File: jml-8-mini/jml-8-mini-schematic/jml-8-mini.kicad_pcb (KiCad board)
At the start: 2 copper layers, 133.1 x 80.5 mm, 47 parts, among them J1 BarrelJack, J2 SIO CHB, J3 UART, J4 CTC Extra Lines, J5 Address Decoding, J6 Z80 Lines, SW1 Reset, SW2 Power, U1 Z80CPU, U10 74LS74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

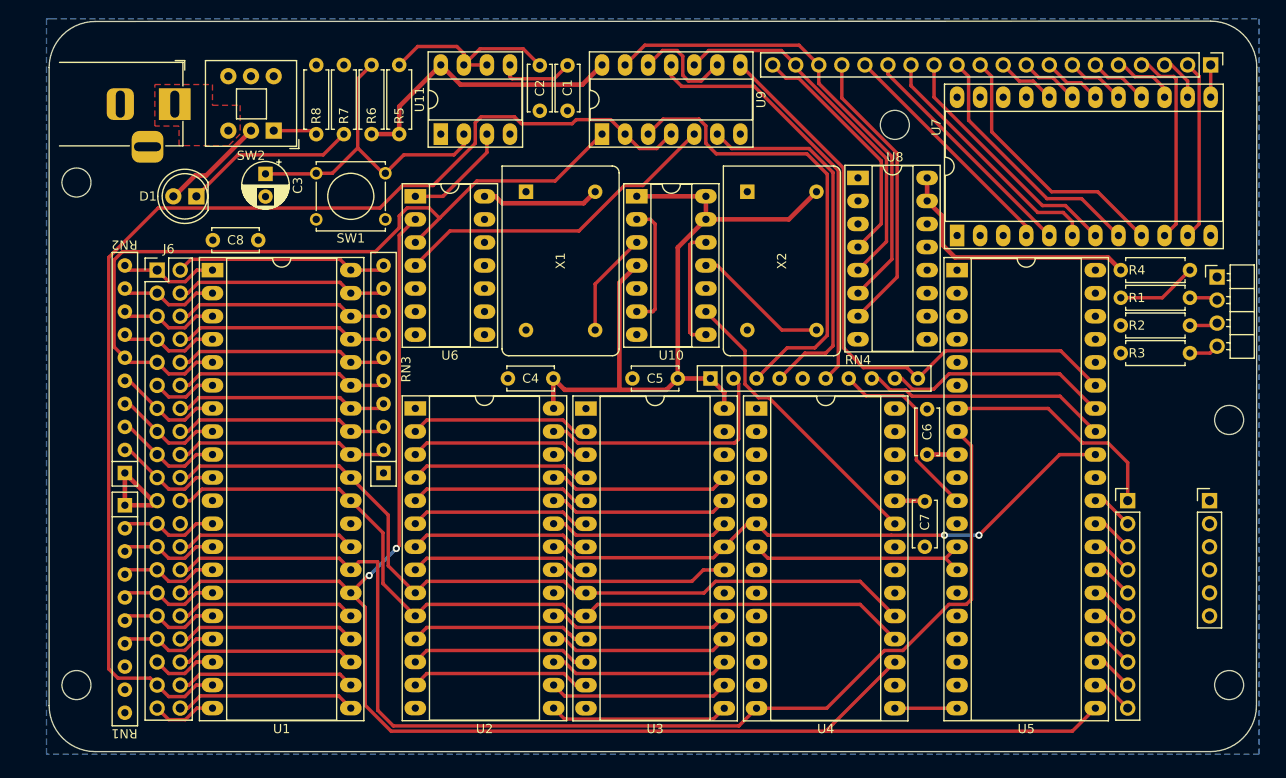
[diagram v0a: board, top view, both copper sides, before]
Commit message: making pcb 4 layers instead of 2, restarting routing, more exact outline dimensions
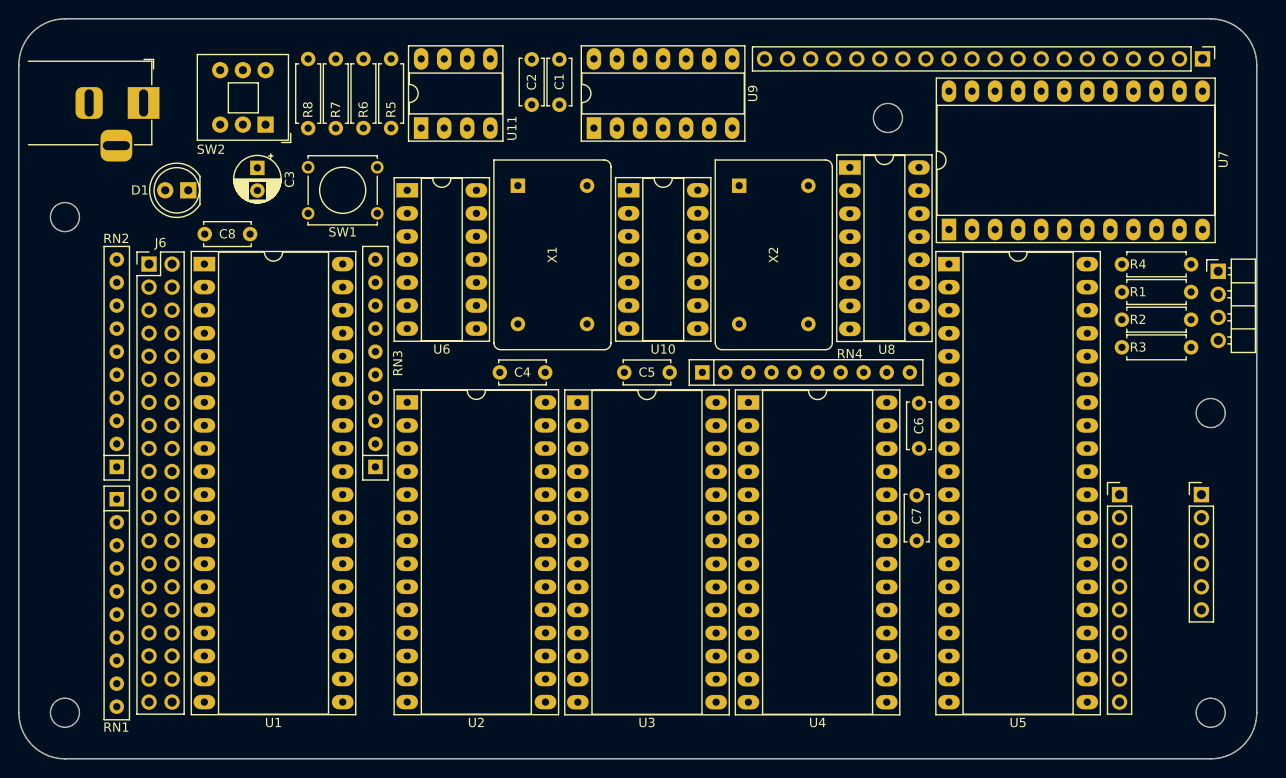
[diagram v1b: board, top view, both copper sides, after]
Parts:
- moved H3 4.02 mm to (88.9, 71.9)
- moved H5 3.66 mm to (215.1, 126.5)
- moved J1 3.44 mm to (97.6, 59.3)
- moved H4 3.30 mm to (88.9, 126.5)
- moved U11 2.26 mm to (128.1, 62.1)
- moved H1 2.17 mm to (215.1, 93.5)
- moved U8 1.45 mm to (175.4, 66.4)
- moved C4 1.11 mm to (141.8, 89.0)
- moved C5 1.11 mm to (155.5, 89.0)
- moved J6 1.11 mm to (98.2, 77.1)
- moved RN1 1.11 mm to (94.6, 103.0)
- moved RN4 1.11 mm to (159.1, 89.0)
- moved U1 1.11 mm to (104.3, 77.1)
- moved U3 1.11 mm to (145.4, 92.3)
- moved U4 1.11 mm to (164.2, 92.3)
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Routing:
- net +5V: track 186.9 -> 0.00 mm
- net /~{RESET}: track 170.5 -> 0.00 mm, vias 2 -> 0
- net /~{MREQ}: track 130.8 -> 0.00 mm
- net /~{M1}: track 130.6 -> 0.00 mm
- net /A0: track 118.6 -> 0.00 mm
- net /A1: track 116.4 -> 0.00 mm
- net /A15: track 87.2 -> 0.00 mm
- net /~{RD}: track 85.8 -> 0.00 mm, vias 2 -> 0
- net /~{SIO}: track 67.9 -> 0.00 mm
- net /Address Decoding/Q2: track 53.2 -> 0.00 mm
- net /~{ROM}: track 51.6 -> 0.00 mm
- net /~{CTC}: track 47.4 -> 0.00 mm
- net /A5: track 43.5 -> 0.00 mm
- net /A3: track 43.5 -> 0.00 mm
- net /A7: track 43.5 -> 0.00 mm
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- added copper zone on In2.Cu, net +5V
- added copper zone on In2.Cu, net /Power, Clock and Reset/PWR_IN
- added copper zone on In1.Cu, net GND
- removed copper zone on F.Cu, net /Power, Clock and Reset/PWR_IN
- removed copper zone on B.Cu, net GND
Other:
- board size 133.1 x 80.5 mm -> 136.4 x 81.5 mm
- copper layers 2 -> 4

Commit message: complete PCB routing
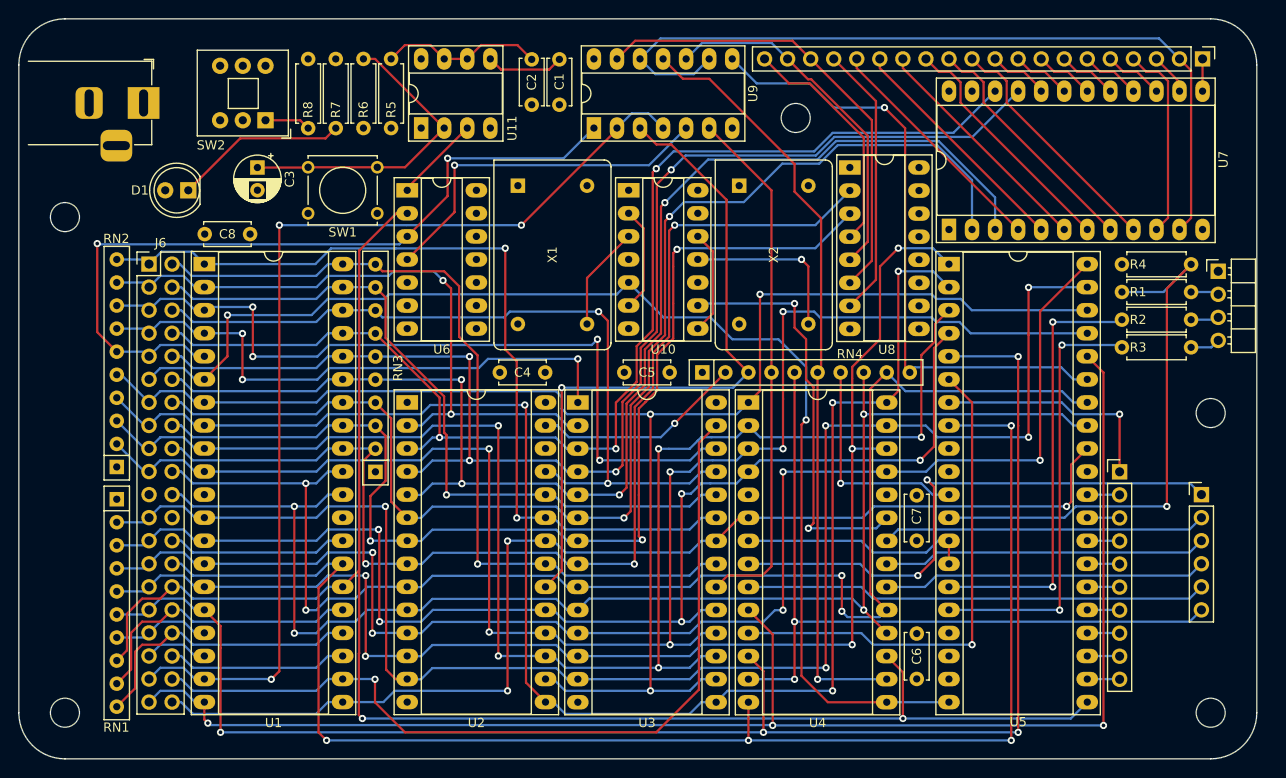
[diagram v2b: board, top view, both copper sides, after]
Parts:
- U4: value Z80 CTC -> Z80CTC
- U5: value Z80 SIO -> Z80SIO
- moved C6 25.4 mm to (182.8, 122.8)
- moved H2 10.2 mm to (169.4, 61.0)
- moved J2 2.51 mm to (205.1, 99.9)
- moved RN3 0.54 mm to (123.1, 99.9)
- moved SW2 0.48 mm to (111.0, 61.2)
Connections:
- J4 pad 1: /Peripherals/CLK/TRG1 -> /Peripherals/ZC/TO1
- J4 pad 2: /Peripherals/ZC/TO1 -> /Peripherals/CLK/TRG1
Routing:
- net /~{RESET}: track 0.00 -> 181.1 mm, vias 0 -> 2
- net /D4: track 0.00 -> 174.3 mm, vias 0 -> 3
- net /D3: track 0.00 -> 174.1 mm, vias 0 -> 4
- net /D6: track 0.00 -> 172.9 mm, vias 0 -> 6
- net /D2: track 0.00 -> 172.4 mm, vias 0 -> 5
- net /~{INT}: track 0.00 -> 171.1 mm, vias 0 -> 4
- net /D5: track 0.00 -> 165.7 mm, vias 0 -> 5
- net /~{IORQ}: track 0.00 -> 163.6 mm, vias 0 -> 3
- net /~{M1}: track 0.00 -> 162.0 mm, vias 0 -> 4
- net /A1: track 0.00 -> 156.1 mm, vias 0 -> 4
- net /A0: track 0.00 -> 154.6 mm, vias 0 -> 4
- net /D0: track 0.00 -> 154.1 mm, vias 0 -> 5
- net /D1: track 0.00 -> 149.2 mm, vias 0 -> 5
- net /A5: track 0.00 -> 148.6 mm, vias 0 -> 4
- net /A6: track 0.00 -> 147.2 mm, vias 0 -> 4
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
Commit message: fix wrong label, add labels and figures to pcb
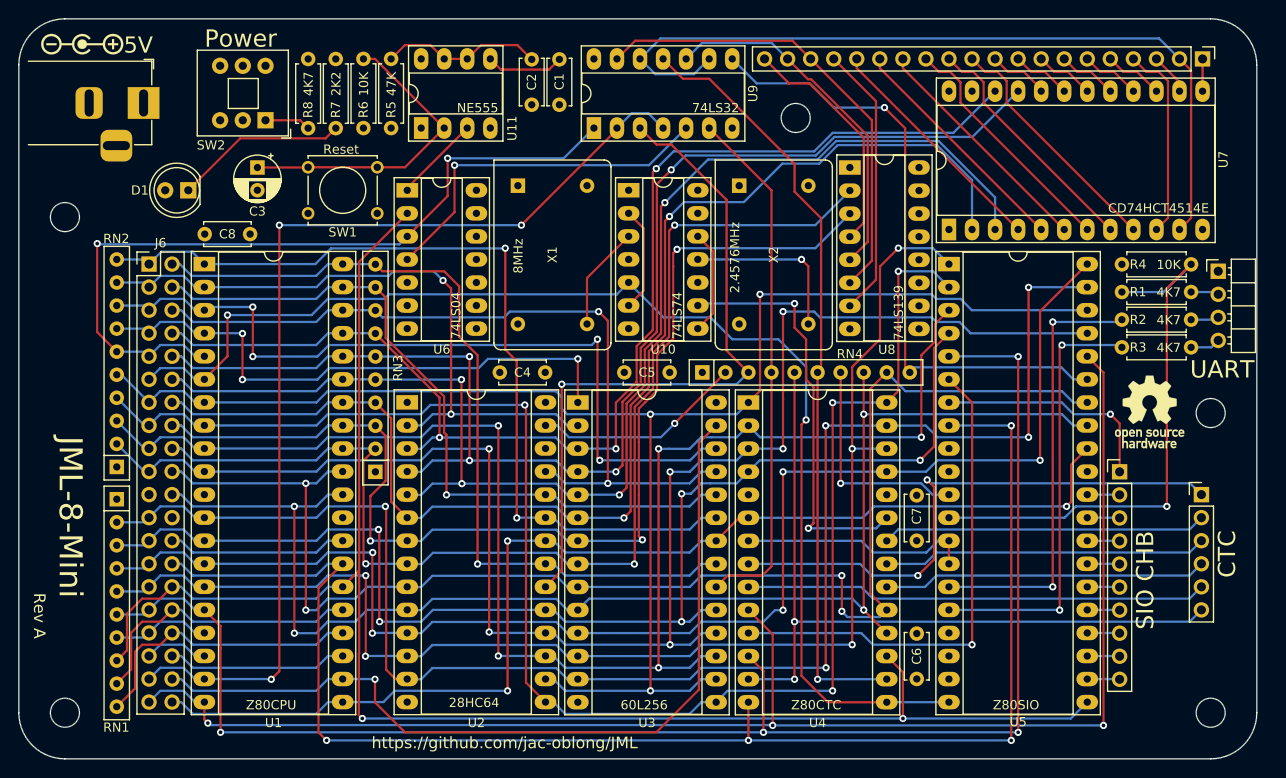
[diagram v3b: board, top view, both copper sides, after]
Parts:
- added REF**: OSHW-Logo_7.5x8mm_SilkScreen, Symbol:OSHW-Logo_7.5x8mm_SilkScreen, F.Cu at (208.4, 93.3)
- added REF**: Polarity_Center_Positive_6mm_SilkScreen, Symbol:Polarity_Center_Positive_6mm_SilkScreen, F.Cu at (90.8, 52.8)
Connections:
- net /Peripherals/CTC_IEO renamed /Peripherals/SIO_IEO
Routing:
- net /~{RESET}: track 181.1 -> 180.4 mm
- net /Peripherals/SIO_IEO: track 25.7 -> 25.1 mm
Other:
- board text added: "1"
- board text added: "10"
- board text added: "10K"
- board text added: "18"
- board text added: "2.4576MHz"
- board text added: "21"
- board text added: "28HC64"
- board text added: "2K2"
- board text added: "30"
- board text added: "47K"
- board text added: "4K7"
- board text added: "5V"
- board text added: "6"
- board text added: "60L256"
- board text added: "7"
- board text added: "74LS04"
- board text added: "74LS139"
- board text added: "74LS32"
- board text added: "74LS74"
- board text added: "8MHz"
- board text added: "CD74HCT4514E"
- board text added: "CTC"
- board text added: "JML-8-Mini"
- board text added: "NE555"
- board text added: "Power"
- board text added: "Reset"
- board text added: "Rev A"
- board text added: "SIO CHB"
- board text added: "UART"
- board text added: "Z80CPU"
- board text added: "Z80CTC"
- board text added: "Z80SIO"
- board text added: "https://github.com/jac-oblong/JML"

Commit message: add JML logo to pcb
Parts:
- added G***: LOGO, LOGO, F.Cu at (88.5, 85.9)
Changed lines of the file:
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@@
     )
+  )
+  (footprint "LOGO" (layer "F.Cu")
+    (at 88.519 85.852 -90)
+    (attr board_only exclude_from_pos_files exclude_from_bom)
+    (fp_text reference "G***" (at 0 0 90) (layer "F.SilkS") hide
+        (effects (font (size 1.5 1.5) (thickness 0.3)))
+    )
+    (fp_text value "LOGO" (at 0.75 0 90) (layer "F.SilkS") hide
+        (effects (font (size 1.5 1.5) (thickness 0.3)))
+    )
+    (fp_poly
+      (pts
+        (xy -4.2 -3.337713)
+        (xy -4.198687 -3.055886)
+        (xy -4.194822 -2.828806)
+        (xy -4.188519 -2.659327)
+        (xy -4.179893 -2.550301)
+        (xy -4.169057 -2.504581)
+        (xy -4.166667 -2.503285)
+        (xy -4.155409 -2.53617)
+        (xy -4.146338 -2.632925)
+        (xy -4.139567 -2.790696)
+        (xy -4.135212 -3.006631)
+        (xy -4.133386 -3.277876)
+        (xy -4.133334 -3.337713)
+        (xy -4.133334 -4.172141)
+        (xy -2.916667 -4.172141)
+        (xy -1.7 -4.172141)
+        (xy -1.7 -3.504599)
+        (xy -1.7 -2.837056)
+        (xy -1.5 -2.837056)
+        (xy -1.3 -2.837056)
+        (xy -1.3 -2.252956)
+        (xy -1.3 -1.668856)
+        (xy -1.066667 -1.668856)
+        (xy -0.833334 -1.668856)
+        (xy -0.833334 -1.084756)
+        (xy -0.833334 -0.500657)
+        (xy -0.6 -0.500657)
+        (xy -0.366667 -0.500657)
+        (xy -0.366667 0.083443)
+        (xy -0.366667 0.667543)
+        (xy -0.016667 0.667543)
+        (xy 0.333333 0.667543)
+        (xy 0.333333 0.083443)
+        (xy 0.333333 -0.500657)
+        (xy 0.566666 -0.500657)
+        (xy 0.8 -0.500657)
+        (xy 0.8 -1.084756)
+        (xy 0.8 -1.668856)
+        (xy 1.033333 -1.668856)
+        (xy 1.266666 -1.668856)
+        (xy 1.266666 -2.252956)
+        (xy 1.266666 -2.837056)
+        (xy 1.45 -2.837056)
+        (xy 1.633333 -2.837056)
+        (xy 1.633333 -3.504599)
+        (xy 1.633333 -4.172141)
+        (xy 2.883333 -4.172141)
+        (xy 4.133333 -4.172141)
+        (xy 4.133333 -3.337713)
+        (xy 4.134647 -3.055886)
+        (xy 4.138512 -2.828806)
+        (xy 4.144814 -2.659327)
+        (xy 4.15344 -2.550301)
+        (xy 4.164276 -2.504581)
+        (xy 4.166666 -2.503285)
+        (xy 4.177924 -2.53617)
+        (xy 4.186996 -2.632925)
+        (xy 4.193766 -2.790696)
+        (xy 4.198121 -3.006631)
+        (xy 4.199948 -3.277876)
+        (xy 4.2 -3.337713)
+        (xy 4.2 -4.172141)
+        (xy 4.766666 -4.172141)
+        (xy 5.333333 -4.172141)
+        (xy 5.333333 -0.834428)
+        (xy 5.333333 2.503286)
+        (xy 7.25 2.503286)
+        (xy 9.166666 2.503286)
+        (xy 9.166666 3.337714)
+        (xy 9.166666 4.172142)
+        (xy 6.683333 4.172142)
+        (xy 4.2 4.172142)
+        (xy 4.2 3.754928)
+        (xy 4.197432 3.574189)
+        (xy 4.190116 3.439781)
+        (xy 4.17863 3.358946)
+        (xy 4.166666 3.337714)
+        (xy 4.152226 3.369847)
+        (xy 4.141487 3.46142)
+        (xy 4.135029 3.605189)
+        (xy 4.133333 3.754928)
+        (xy 4.133333 4.172142)
+        (xy 3.55 4.172142)
+        (xy 2.966666 4.172142)
+        (xy 2.966666 1.251643)
+        (xy 2.966666 -1.668856)
+        (xy 2.7 -1.668856)
+        (xy 2.433333 -1.668856)
+        (xy 2.433333 -1.084756)
+        (xy 2.433333 -0.500657)
+        (xy 2.2 -0.500657)
+        (xy 1.966666 -0.500657)
+        (xy 1.966666 0.083443)
+        (xy 1.966666 0.667543)
+        (xy 1.733333 0.667543)
+        (xy 1.5 0.667543)
+        (xy 1.5 1.251643)
+        (xy 1.5 1.835743)
+        (xy 1.266666 1.835743)
+        (xy 1.033333 1.835743)
+        (xy 1.033333 2.419843)
+        (xy 1.033333 3.003943)
+        (xy 0.8 3.003943)
+        (xy 0.566666 3.003943)
+        (xy 0.566666 3.588042)
+        (xy 0.566666 4.172142)
+        (xy -0.016667 4.172142)
+        (xy -0.6 4.172142)
+        (xy -0.6 3.588042)
+        (xy -0.6 3.003943)
+        (xy -0.833334 3.003943)
+        (xy -1.066667 3.003943)
+        (xy -1.066667 2.419843)
+        (xy -1.066667 1.835743)
+        (xy -1.3 1.835743)
+        (xy -1.533334 1.835743)
+        (xy -1.533334 1.251643)
+        (xy -1.533334 0.667543)
+        (xy -1.766667 0.667543)
+        (xy -2 0.667543)
+        (xy -2 0.083443)
+        (xy -2 -0.500657)
+        (xy -2.233334 -0.500657)
+        (xy -2.466667 -0.500657)
+        (xy -2.466667 -1.084756)
+        (xy -2.466667 -1.668856)
+        (xy -2.733334 -1.668856)
+        (xy -3 -1.668856)
+        (xy -3 1.251643)
+        (xy -3 4.172142)
+        (xy -3.566667 4.172142)
+        (xy -4.133334 4.172142)
+        (xy -4.133334 3.754928)
+        (xy -4.135901 3.574189)
+        (xy -4.143217 3.439781)
+        (xy -4.154704 3.358946)
+        (xy -4.166667 3.337714)
+        (xy -4.181107 3.369847)
+        (xy -4.191846 3.46142)
+        (xy -4.198304 3.605189)
+        (xy -4.2 3.754928)
+        (xy -4.2 4.172142)
+        (xy -6.683334 4.172142)
+        (xy -9.166667 4.172142)
+        (xy -9.166667 3.337714)
+        (xy -9.166667 2.503286)
+        (xy -7.25 2.503286)
+        (xy -5.333334 2.503286)
+        (xy -5.333334 -0.834428)
+        (xy -5.333334 -4.172141)
+        (xy -4.766667 -4.172141)
+        (xy -4.2 -4.172141)
+      )
+      (stroke (width 0) (type solid)) (fill solid) (layer "F.SilkS"))
   )
   (footprint "Resistor_THT:R_Axial_DIN0207_L6.3mm_D2.5mm_P7.62mm_Horizontal" (layer "F.Cu")

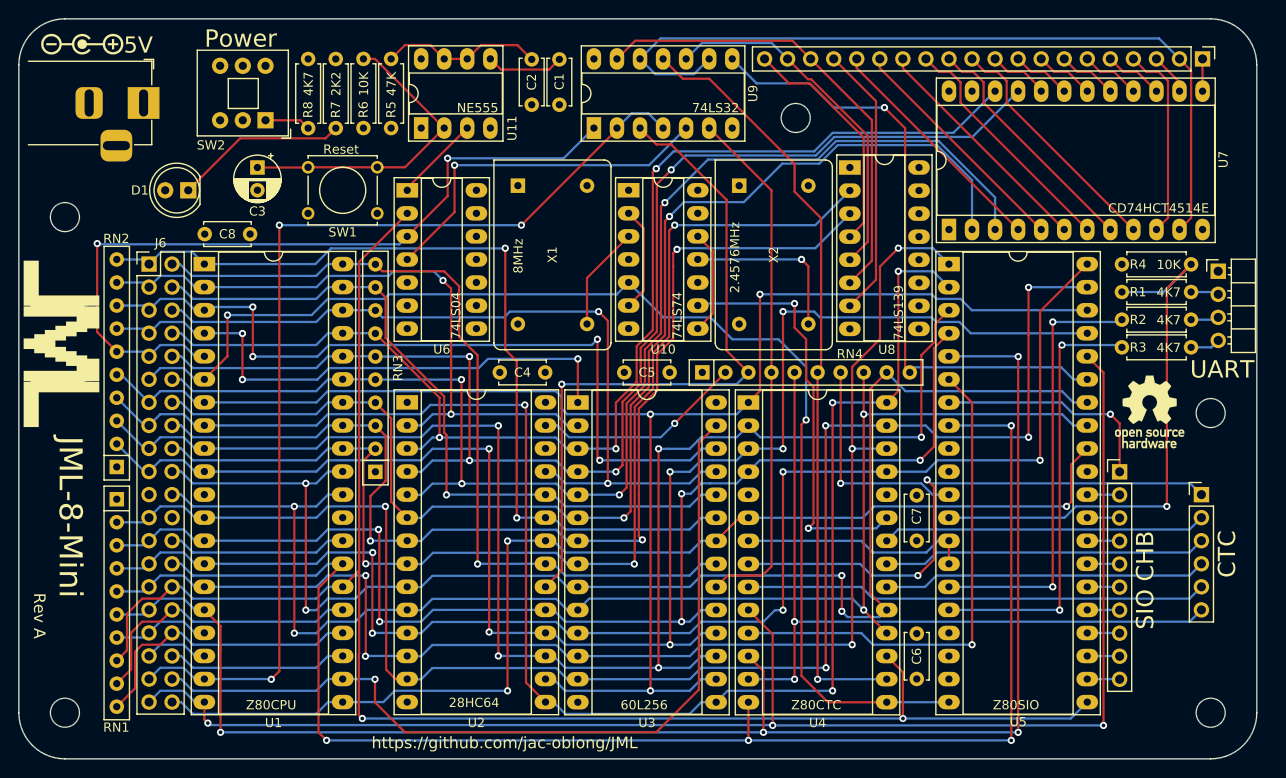
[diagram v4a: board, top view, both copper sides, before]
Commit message: new symbol & footprint for logo, add to schematic and pcb
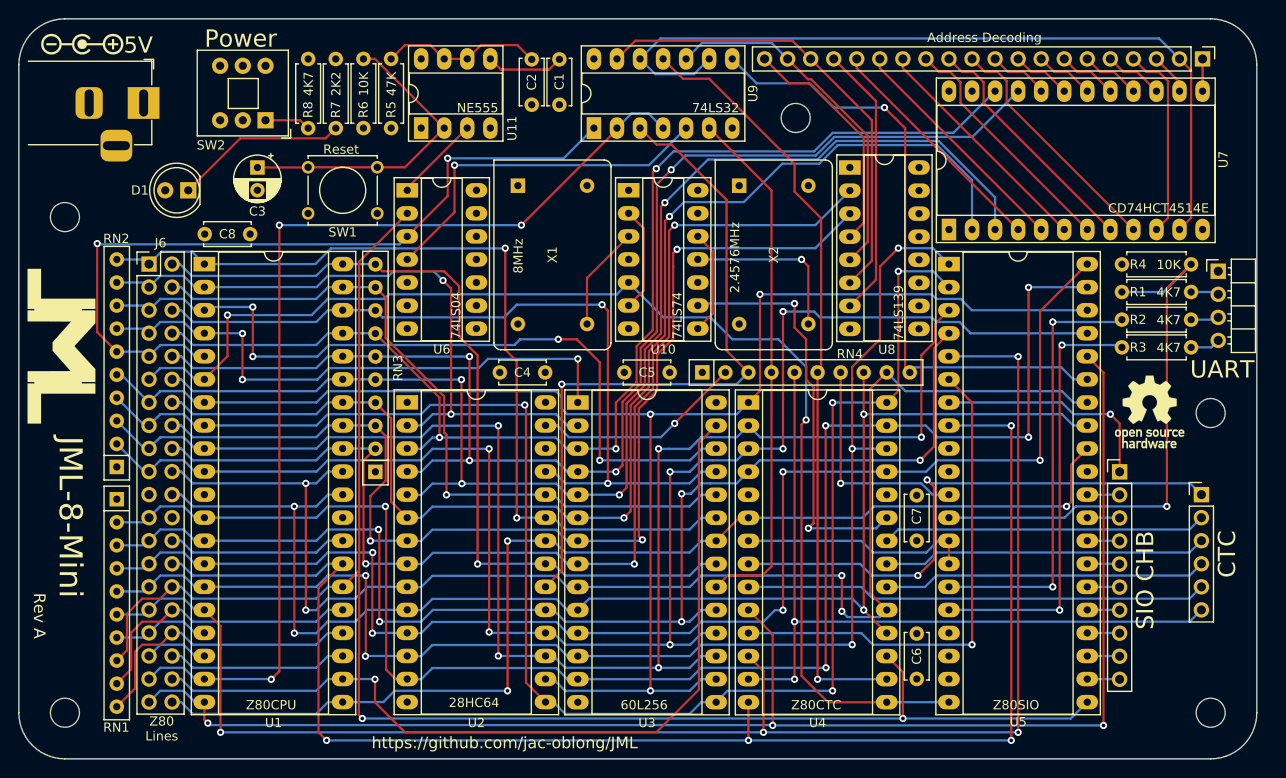
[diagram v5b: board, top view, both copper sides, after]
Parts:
- removed the G*** at (88.5, 85.9)
- added G***: LOGO, JML:JML-Logo, F.Cu at (88.5, 86.9)
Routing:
- net /A13: track 87.4 -> 86.1 mm
- net /A8: track 88.1 -> 89.4 mm
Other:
- board text added: "Address Decoding"
- board text added: "Z80 Lines"
